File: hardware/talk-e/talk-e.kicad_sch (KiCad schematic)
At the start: 20 parts, among them J1 Conn_01x04_Socket, Q1 FS8205A, U1 RFM96W-433S2, U2 DW01A, U3 TP4056-42-ESOP8, U4 ESP32-S3

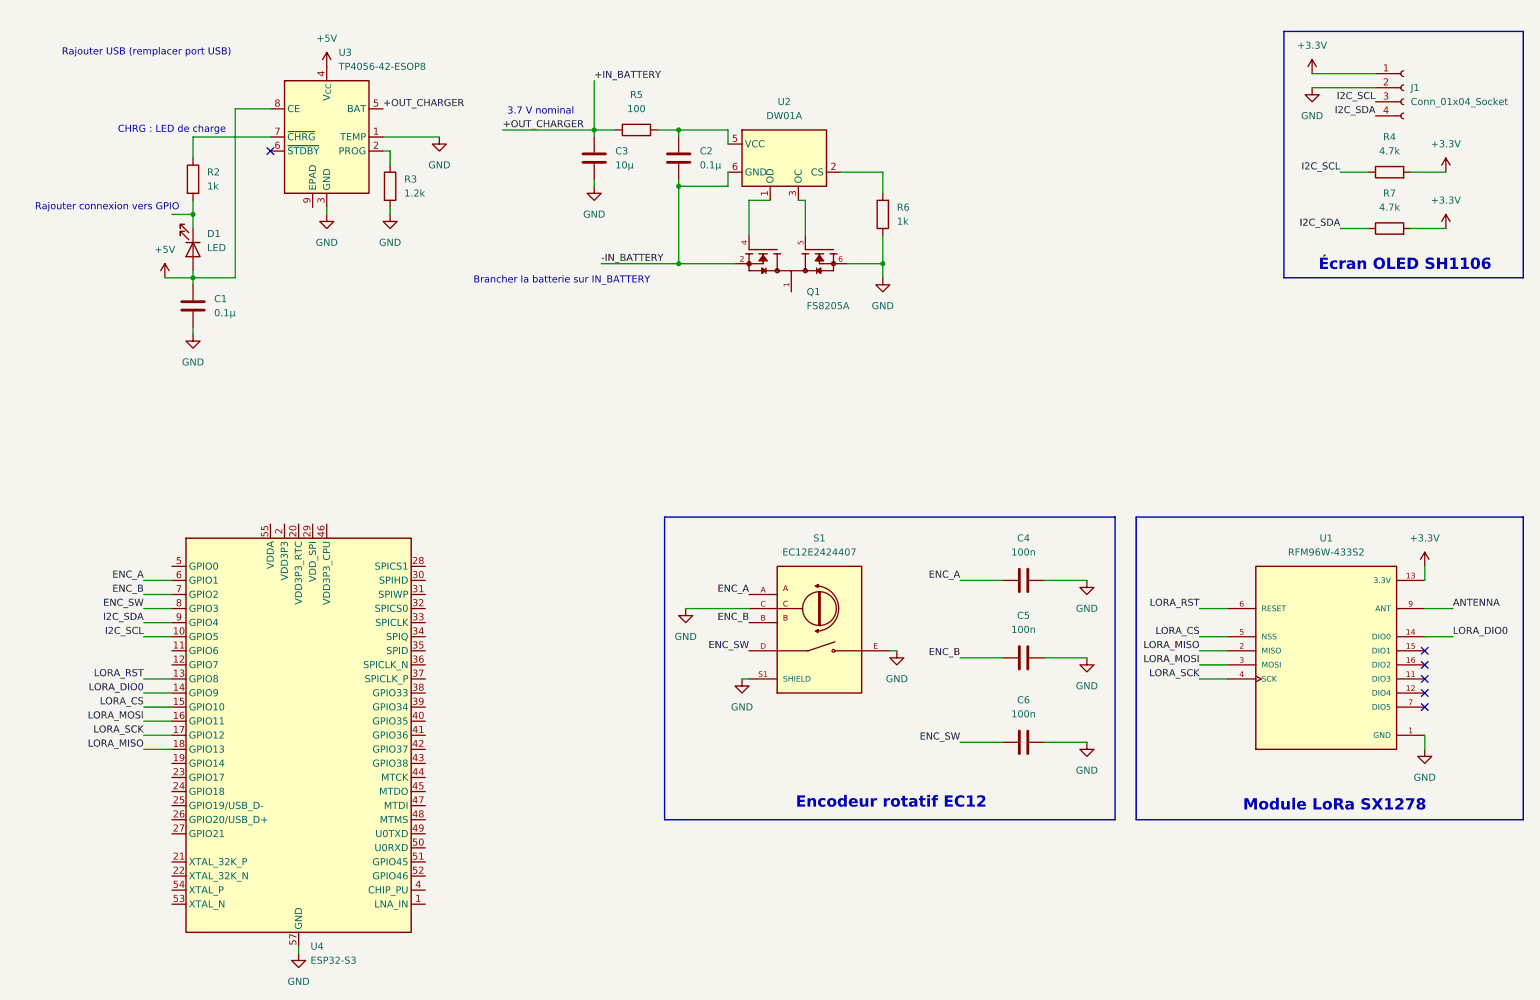
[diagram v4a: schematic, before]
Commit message: Added 3 buttons and power switch
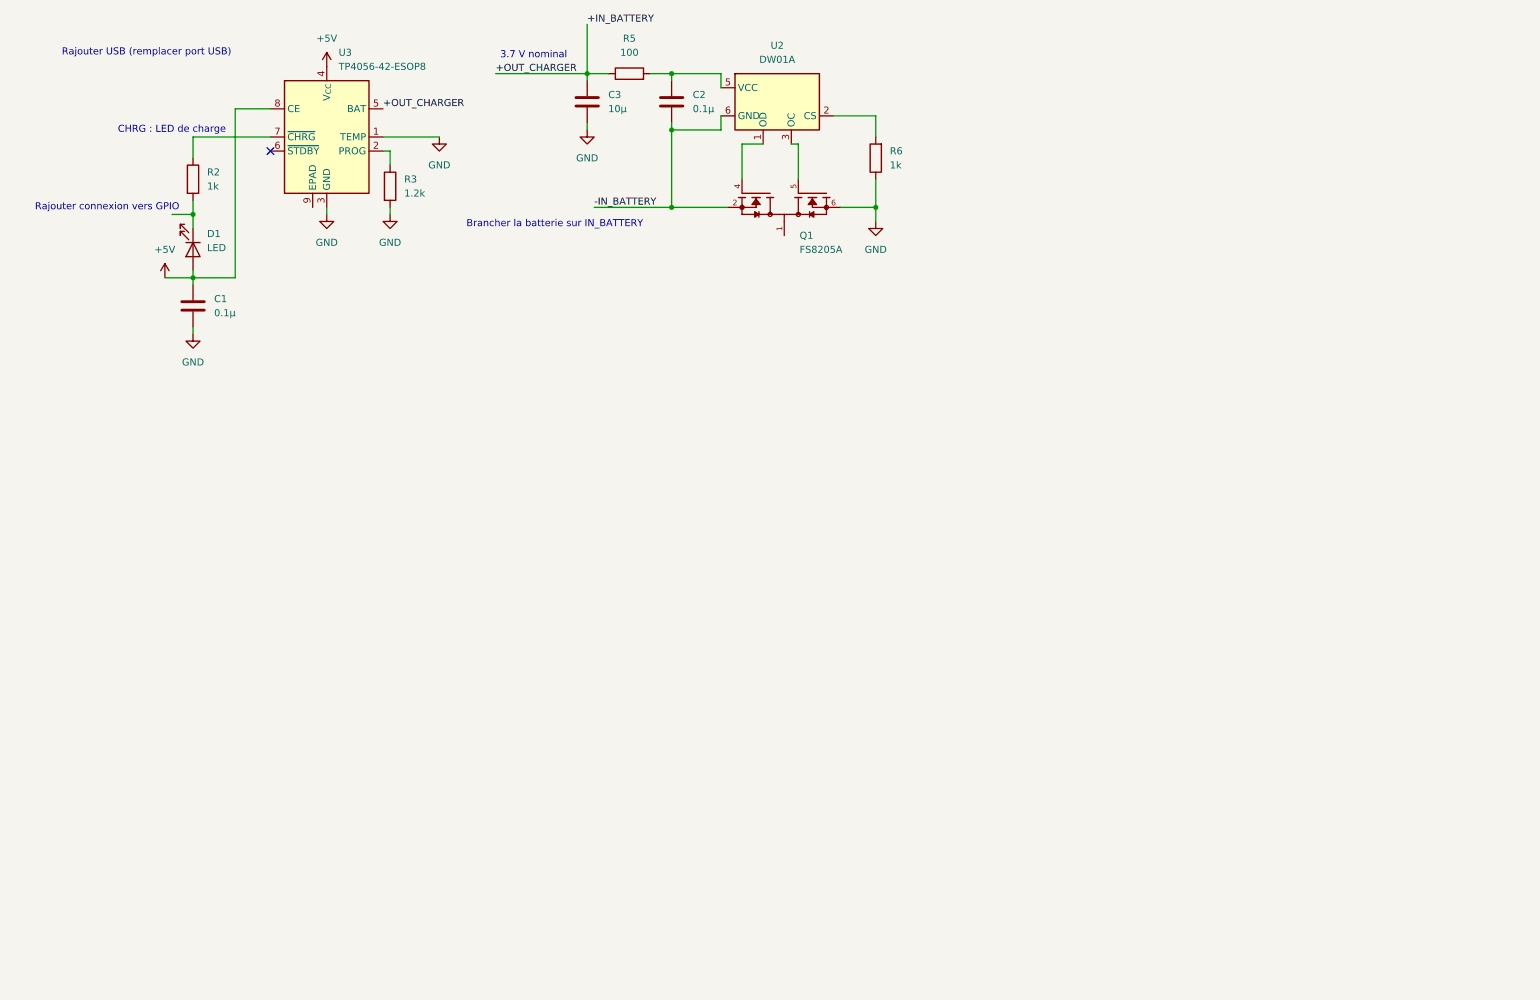
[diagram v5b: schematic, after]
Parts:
- removed C4, C5, C6: 100n, symbol Device:C
- removed J1: Conn_01x04_Socket, Connector_PinSocket_2.54mm:PinSocket_1x04_P2.54mm_Vertical, symbol Connector:Conn_01x04_Socket
- removed R4, R7: 4.7k, symbol Device:R
- removed S1: EC12E2424407, EC12E2424407:ALPS_EC12E2424407, symbol EC12E2424407:EC12E2424407
- removed U1: RFM96W-433S2, RFM96W-433S2:MODULE_RFM96W-433S2, symbol RFM96W-433S2:RFM96W-433S2
- removed U4: ESP32-S3, Package_DFN_QFN:QFN-56-1EP_7x7mm_P0.4mm_EP4x4mm, symbol MCU_Espressif:ESP32-S3
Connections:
- no-connect marks 6 -> 1
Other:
- note removed: "Encodeur rotatif EC12"
- note removed: "Module LoRa SX1278"
- note removed: "Écran OLED SH1106"
- moved on the sheet: C2, C3, Q1, R5, R6, U2

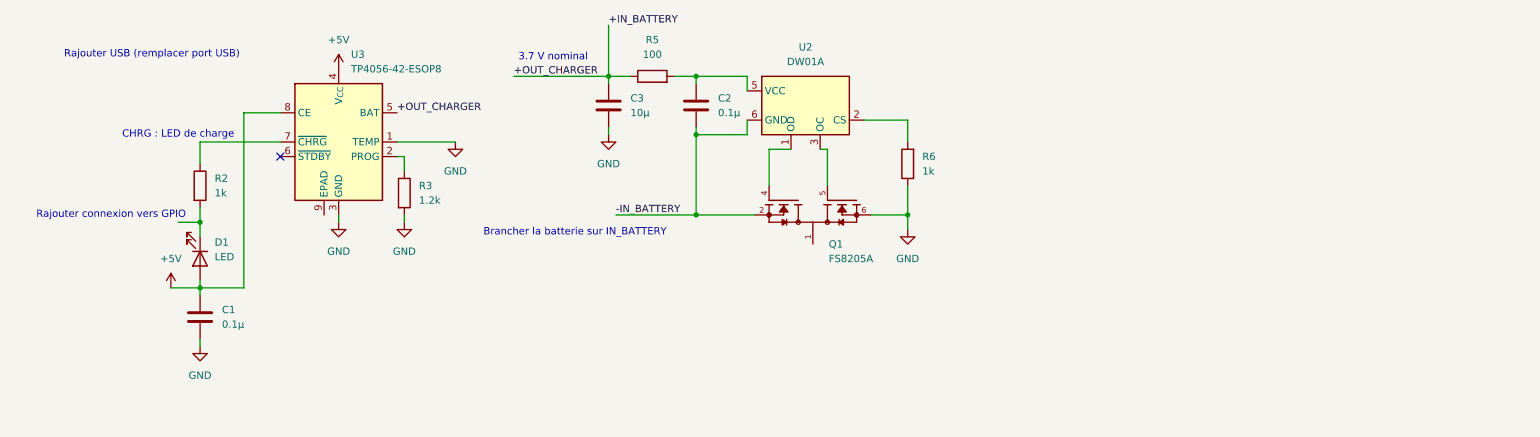
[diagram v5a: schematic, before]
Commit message: Added TP4056, DW01A, AP2112K-3.3 to schematic
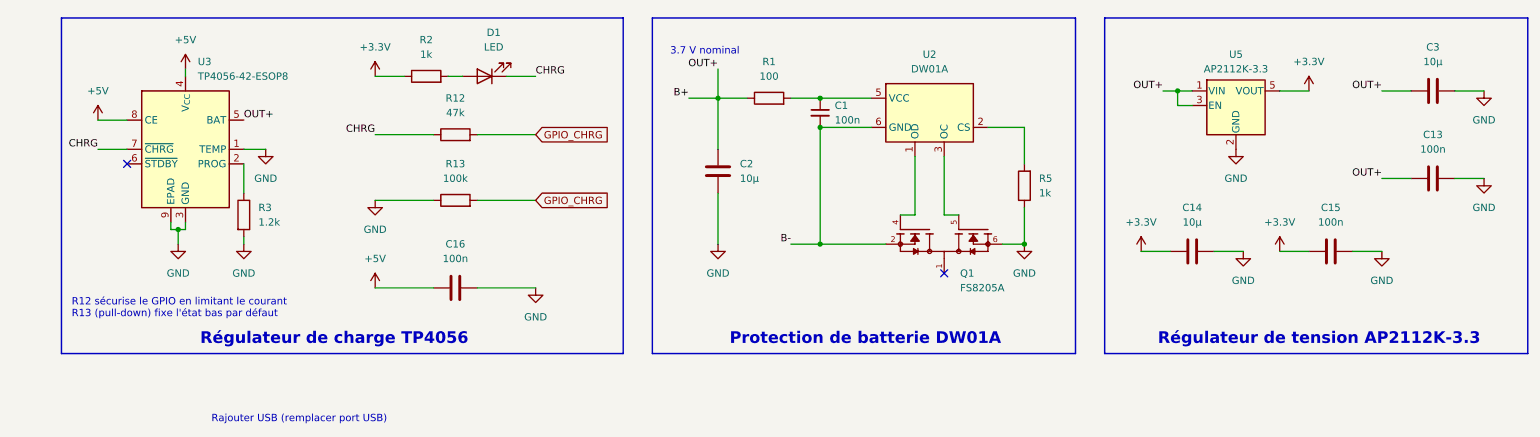
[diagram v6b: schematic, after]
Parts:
- removed C1: 0.1µ, symbol Device:C
- removed R6: 1k, symbol Device:R
- added C1: 100n, symbol Device:C_Small
- added C13, C15, C16: 100n, symbol Device:C
- added C14: 10µ, symbol Device:C
- added R1: 100, symbol Device:R
- added R12: 47k, symbol Device:R
- added R13: 100k, symbol Device:R
- added U5: AP2112K-3.3, Package_TO_SOT_SMD:SOT-23-5, symbol Regulator_Linear:AP2112K-3.3
- C2: value 0.1µ -> 10µ
- R5: value 100 -> 1k
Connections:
- net +5V: now also C16.1; no longer D1.2 (A)
- net GND: now also C2.2, R5.1, U3.9 (EPAD), C13.2, C14.2, C15.2, C16.2, R13.1, U5.2 (GND)
- net at R2.2: now also D1.2 (A); no longer D1.1 (K)
- net at U2.2 (CS): now also R5.2
- net +3.3V: now reaches R2.1
- net +3.3V: now also C14.1, C15.1, U5.5 (VOUT); no longer U3.7 (~{CHRG})
- net +IN_BATTERY renamed B+
- net B+: now also C2.1, C13.1, R1.1, U5.1 (VIN), U5.3 (EN); no longer R5.1
- net -IN_BATTERY renamed B-
- net B-: now also C1.2; no longer C2.2
- new net: C1.1, R1.2, U2.5 (VCC)
- new net CHRG: D1.1 (K), R12.1, U3.7 (~{CHRG})
- new net GPIO_CHRG: R12.2, R13.2
- no-connect marks 1 -> 2
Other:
- note added: "Protection de batterie DW01A"
- note added: "R12 sécurise le GPIO en limitant le courant R13 (pull-down) fixe l'état bas par défaut"
- note added: "Régulateur de charge TP4056"
- note added: "Régulateur de tension AP2112K-3.3"
- note removed: "Brancher la batterie sur IN_BATTERY"
- note removed: "CHRG : LED de charge"
- note removed: "Rajouter connexion vers GPIO"
- moved on the sheet: D1, R2, R3, U3

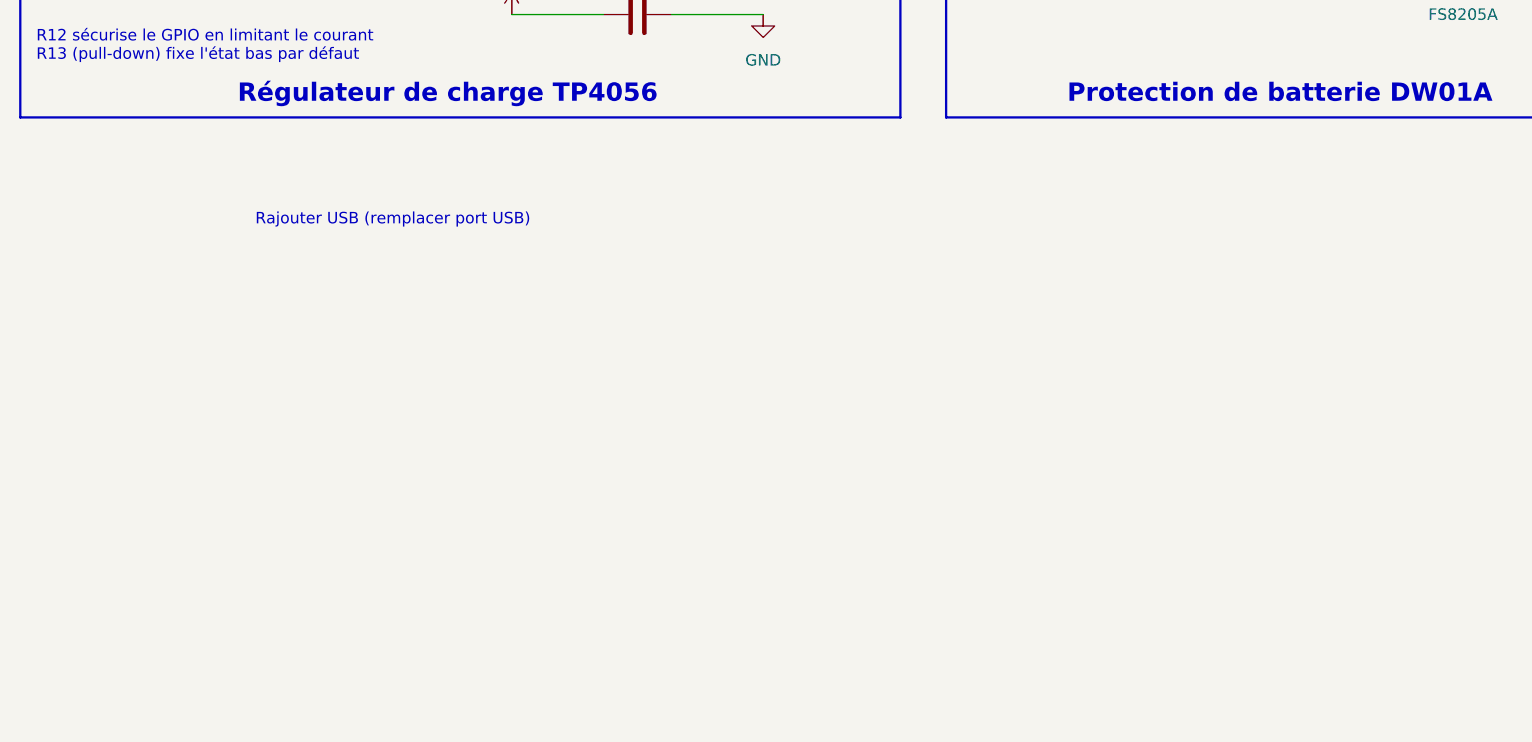
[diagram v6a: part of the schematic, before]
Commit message: Added UART IDC connector, ESP32 decoupling capacitors
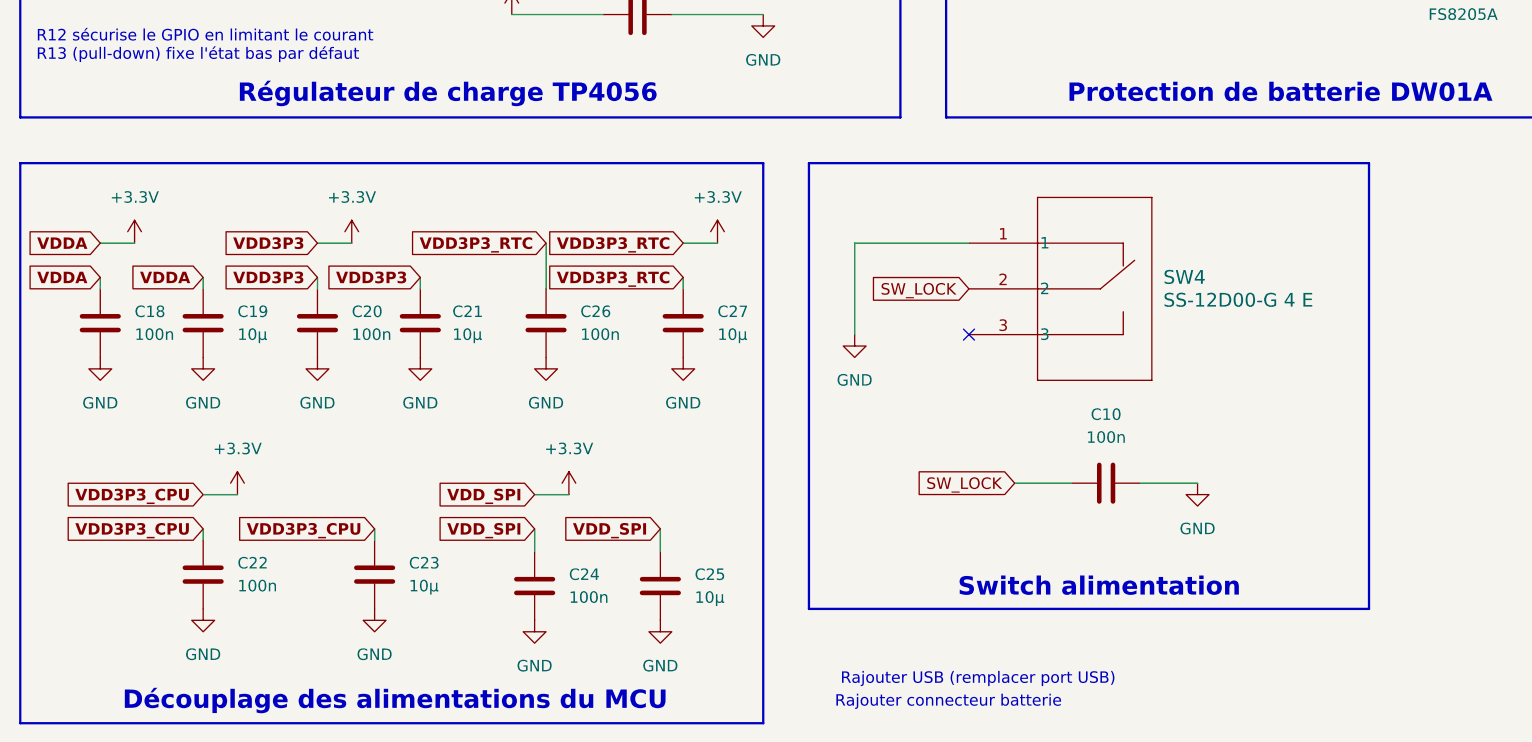
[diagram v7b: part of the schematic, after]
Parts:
- added C10, C18, C20, C22, C24, C26: 100n, symbol Device:C
- added C19, C21, C23, C25, C27: 10µ, symbol Device:C
- added SW4: SS-12D00-G 4 E, 1P2T_SS-12D00_CNK, symbol 2026-05-09_16-09-49:SS-12D00-G_4_E
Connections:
- net +3.3V: now also C18.2, C19.2, C20.2, C21.2, C22.2, C23.2, C24.2, C25.2, C26.2, C27.2
- net GND: now also C10.2, C18.1, C19.1, C20.1, C21.1, C22.1, C23.1, C24.1, C25.1, C26.1, C27.1, SW4.1
- new net SW_LOCK: C10.1, SW4.2
- no-connect marks 2 -> 3
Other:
- note added: "Découplage des alimentations du MCU"
- note added: "Rajouter connecteur batterie"
- note added: "Switch alimentation"

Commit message: Something moved in the schematic but idk what
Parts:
- added C12: 100n, symbol Device:C
- added R9: 10k, symbol Device:R
- added SW5: SW_Push, symbol Switch:SW_Push
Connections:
- net +3.3V: now also R9.2
- net GND: now also C12.2, SW5.2
- new net RESET: C12.1, R9.1, SW5.1
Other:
- note added: "Bouton RESET"
